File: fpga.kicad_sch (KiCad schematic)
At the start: 29 parts, among them U10 P0082_BOTTOMMOUNT, U11 SN75160BDW, U12 SN75160BDW, U13 SN75160BDW, U14 SN75160BDW

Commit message: Save work on simplifying the desing
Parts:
- removed U11, U12, U13, U14: SN75160BDW, Package_SO:SOIC-20W_7.5x12.8mm_P1.27mm, symbol Interface:SN75160BDW
- added R55, R56, R57, R58: 0R, Resistor_SMD:R_0402_1005Metric_Pad0.72x0.64mm_HandSolder, symbol Device:R
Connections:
- net D_ADC_A0: now also R95.1
- net D_ADC_A1: now also R96.1
- net D_ADC_A10: now also R105.1
- net D_ADC_A11: now also R106.1
- net D_ADC_A2: now also R97.1
- net D_ADC_A3: now also R98.1
- net D_ADC_A4: now also R99.1
- net D_ADC_A5: now also R100.1
- net D_ADC_A6: now also R101.1
- net D_ADC_A7: now also R102.1
- net D_ADC_A8: now also R103.1
- net D_ADC_A9: now also R104.1
- net D_ADC_B0: now also R107.1
- net D_ADC_B1: now also R108.1
- net D_ADC_B10: now also R117.1
- net D_ADC_B11: now also R118.1
- net D_ADC_B2: now also R109.1
- net D_ADC_B3: now also R110.1
- net D_ADC_B4: now also R111.1
- net D_ADC_B5: now also R112.1
- net D_ADC_B6: now also R113.1
- net D_ADC_B7: now also R114.1
- net D_ADC_B8: now also R115.1
- net D_ADC_B9: now also R116.1
- net at U10.JP1_11 (GPIO-0_VCC_SYS): now also R55.1
- net GND: now reaches U10.JP1_12 (GPIO-0_GND), U10.JP1_30 (GPIO-0_GND)
- net GND: now also U10.JP2_12 (GPIO-1_GND), U10.JP2_30 (GPIO-1_GND)
- net at U10.JP1_29 (GPIO-0_VCC3P3): now also R56.1
- net at U10.JP2_11 (GPIO-1_VCC_SYS): now also R57.1
- net at U10.JP2_29 (GPIO-1_VCC3P3): now also R58.1
- new net +3V3: R56.2, R58.2
- new net +5V: R55.2, R57.2
- no-connect marks 16 -> 0
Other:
- moved on the sheet: R100, R101, R102, R103, R104, R105, R106, R107, R108, R109, R110, R111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

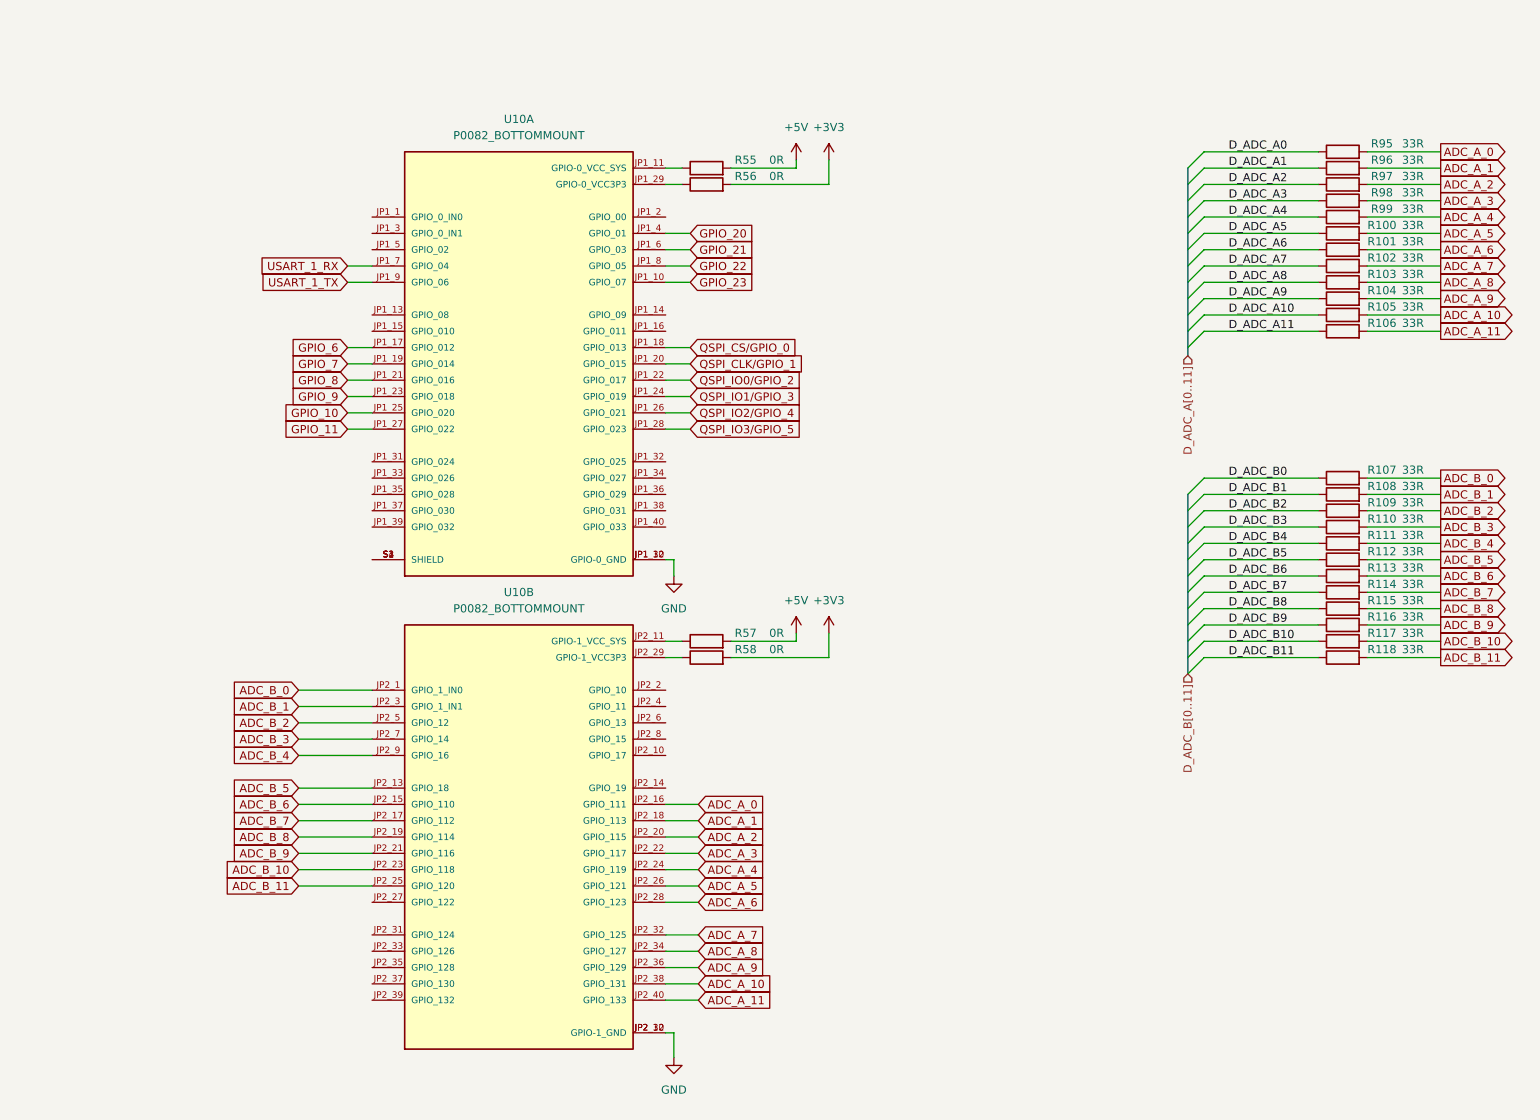
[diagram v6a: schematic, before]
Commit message: Simplifying the design
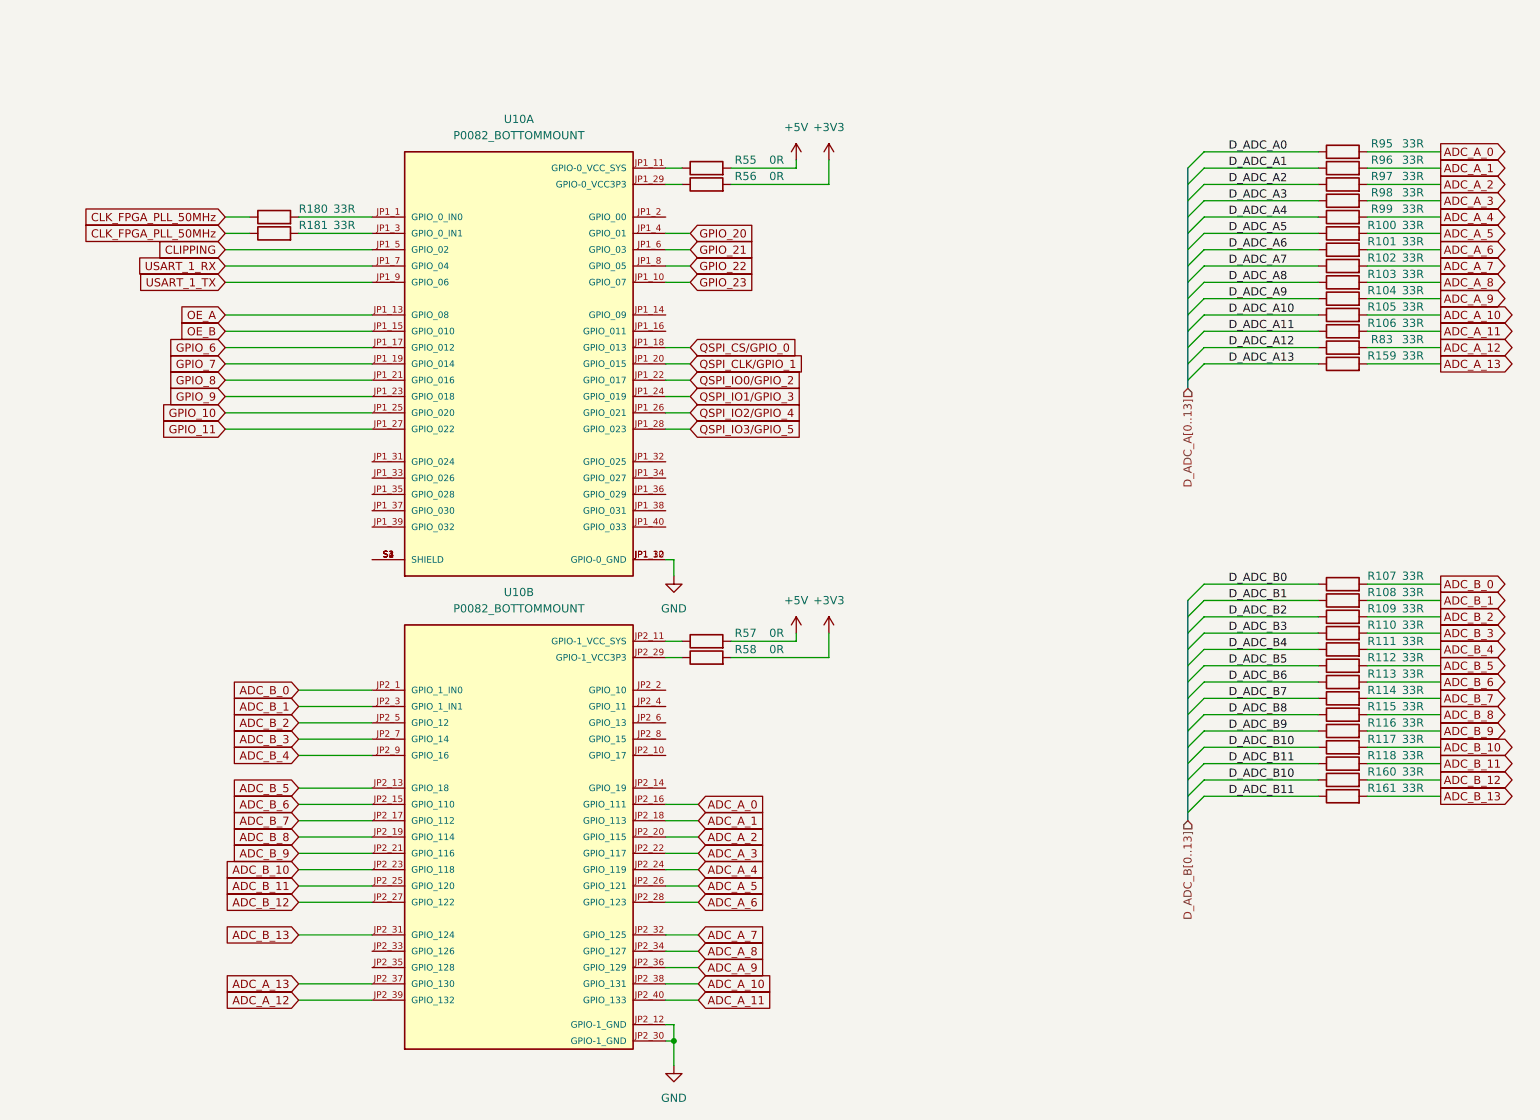
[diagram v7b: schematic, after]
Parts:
- added R159, R160, R161, R180, R181, R83: 33R, Resistor_SMD:R_0402_1005Metric_Pad0.72x0.64mm_HandSolder, symbol Device:R
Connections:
- net D_ADC_B10: now also R160.1
- net D_ADC_B11: now also R161.1
- net at U10.JP1_1 (GPIO_0_IN0): now also R180.2
- net OE_A: now reaches U10.JP1_13 (GPIO_08)
- net OE_B: now reaches U10.JP1_15 (GPIO_010)
- net at U10.JP1_3 (GPIO_0_IN1): now also R181.2
- net CLIPPING: now reaches U10.JP1_5 (GPIO_02)
- net ADC_B_12: now reaches U10.JP2_27 (GPIO_122)
- net ADC_B_12: now also R160.2
- net ADC_B_13: now reaches U10.JP2_31 (GPIO_124)
- net ADC_B_13: now also R161.2
- net ADC_A_13: now reaches U10.JP2_37 (GPIO_130)
- net ADC_A_13: now also R159.2
- net ADC_A_12: now reaches U10.JP2_39 (GPIO_132)
- net ADC_A_12: now also R83.2
- new net CLK_FPGA_PLL_50MHz: R180.1, R181.1
- new net D_ADC_A12: R83.1
- new net D_ADC_A13: R159.1
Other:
- moved on the sheet: R107, R108, R109, R110, R111, R112, R113, R114, R115, R116, R117, R118

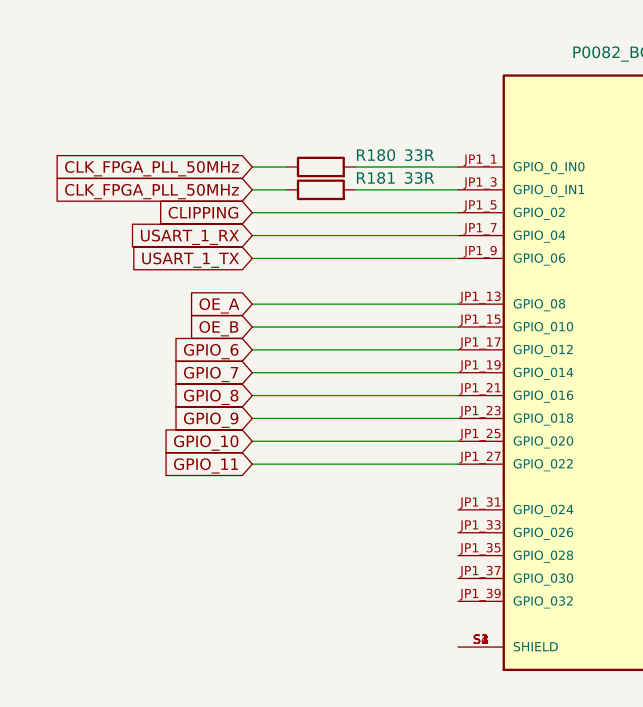
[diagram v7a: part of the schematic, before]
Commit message: Gain on diff amp 0.2
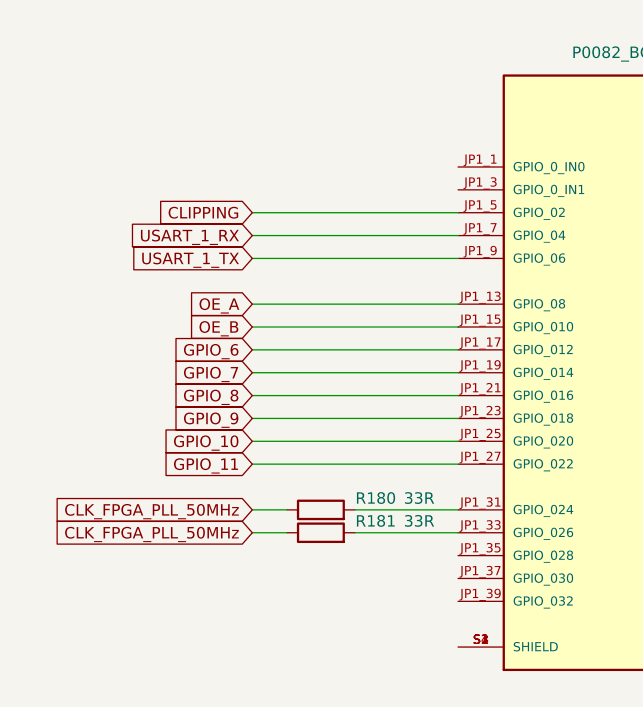
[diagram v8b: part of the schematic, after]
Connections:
- net at R181.2: now also U10.JP1_33 (GPIO_026); no longer U10.JP1_3 (GPIO_0_IN1)
- net at U10.JP1_1 (GPIO_0_IN0): no longer R180.2
- net at U10.JP1_31 (GPIO_024): now also R180.2
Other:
- moved on the sheet: R180, R181
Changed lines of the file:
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@@
 	(wire
 		(pts
-			(xy 234.95 54.61) (xy 246.38 54.61)
+			(xy 68.58 87.63) (xy 80.01 87.63)
 		)
 		(stroke
@@
 	(wire
 		(pts
-			(xy 130.81 143.51) (xy 125.73 143.51)
+			(xy 234.95 54.61) (xy 246.38 54.61)
 		)
 		(stroke
@@
 	(wire
 		(pts
-			(xy 68.58 135.89) (xy 80.01 135.89)
+			(xy 130.81 143.51) (xy 125.73 143.51)
 		)
 		(stroke
@@
 	(wire
 		(pts
-			(xy 130.81 140.97) (xy 125.73 140.97)
+			(xy 68.58 135.89) (xy 80.01 135.89)
 		)
 		(stroke
@@
 	(wire
 		(pts
-			(xy 129.54 77.47) (xy 125.73 77.47)
+			(xy 130.81 140.97) (xy 125.73 140.97)
 		)
 		(stroke
@@
 	(wire
 		(pts
-			(xy 68.58 46.99) (xy 80.01 46.99)
+			(xy 129.54 77.47) (xy 125.73 77.47)
 		)
 		(stroke
@@
 	(wire
 		(pts
-			(xy 60.96 46.99) (xy 57.15 46.99)
-		)
-		(stroke
-			(width 0)
-			(type default)
-		)
-	)
-	(wire
-		(pts
 			(xy 209.55 67.31) (xy 227.33 67.31)
 		)
@@
 		)
 	)
-	(wire
-		(pts
-			(xy 60.96 49.53) (xy 57.15 49.53)
-		)
-		(stroke
-			(width 0)
-			(type default)
-		)
-	)
 	(bus
 		(pts
@@
 	(wire
 		(pts
-			(xy 68.58 49.53) (xy 80.01 49.53)
-		)
-		(stroke
-			(width 0)
-			(type default)
-		)
-	)
-	(wire
-		(pts
 			(xy 68.58 140.97) (xy 80.01 140.97)
 		)
@@
 	(wire
 		(pts
+			(xy 60.96 85.09) (xy 57.15 85.09)
+		)
+		(stroke
+			(width 0)
+			(type default)
+		)
+	)
+	(wire
+		(pts
+			(xy 60.96 87.63) (xy 57.15 87.63)
+		)
+		(stroke
+			(width 0)
+			(type default)
+		)
+	)
+	(wire
+		(pts
 			(xy 130.81 161.29) (xy 125.73 161.29)
 		)
@@
 		)
 	)
+	(wire
+		(pts
+			(xy 68.58 85.09) (xy 80.01 85.09)
+		)
+		(stroke
+			(width 0)
+			(type default)
+		)
+	)
 	(bus
 		(pts
@@
 		)
 	)
-	(global_label "CLK_FPGA_PLL_50MHz"
+	(global_label "OE_B"
 		(shape input)
-		(at 57.15 46.99 180)
+		(at 57.15 64.77 180)
 		(fields_autoplaced yes)
 		(effects
@@
 		)
 		(property "Intersheetrefs" "${INTERSHEET_REFS}"
-			(at 33.4215 46.99 0)
+			(at 49.4477 64.77 0)
 			(effects
 				(font
@@
 		)
 	)
-	(global_label "OE_B"
-		(shape input)
-		(at 57.15 64.77 180)
+	(global_label "ADC_B_11"
+		(shape output)
+		(at 246.38 132.08 0)
 		(fields_autoplaced yes)
 		(effects
@@
 				(size 1.27 1.27)
 			)
-			(justify right)
+			(justify left)
 		)
 		(property "Intersheetrefs" "${INTERSHEET_REFS}"
-			(at 49.4477 64.77 0)
+			(at 258.618 132.08 0)
 			(effects
 				(font
 					(size 1.27 1.27)
 				)
-				(justify right)
+				(justify left)
 				(hide yes)
 			)
 		)
 	)
-	(global_label "ADC_B_11"
+	(global_label "ADC_A_10"
 		(shape output)
-		(at 246.38 132.08 0)
+		(at 246.38 62.23 0)
 		(fields_autoplaced yes)
 		(effects
@@
 		)
 		(property "Intersheetrefs" "${INTERSHEET_REFS}"
-			(at 258.618 132.08 0)
+			(at 258.4366 62.23 0)
 			(effects
 				(font
@@
 		)
 	)
-	(global_label "ADC_A_10"
-		(shape output)
-		(at 246.38 62.23 0)
+	(global_label "CLK_FPGA_PLL_50MHz"
+		(shape input)
+		(at 57.15 87.63 180)
 		(fields_autoplaced yes)
 		(effects
@@
 				(size 1.27 1.27)
 			)
-			(justify left)
+			(justify right)
 		)
 		(property "Intersheetrefs" "${INTERSHEET_REFS}"
-			(at 258.4366 62.23 0)
+			(at 33.4215 87.63 0)
 			(effects
 				(font
 					(size 1.27 1.27)
 				)
-				(justify left)
+				(justify right)
 				(hide yes)
 			)
@@
 		)
 	)
-	(global_label "CLK_FPGA_PLL_50MHz"
+	(global_label "QSPI_IO3{slash}GPIO_5"
 		(shape input)
-		(at 57.15 49.53 180)
+		(at 129.54 80.01 0)
 		(fields_autoplaced yes)
 		(effects
@@
 				(size 1.27 1.27)
 			)
-			(justify right)
+			(justify left)
 		)
 		(property "Intersheetrefs" "${INTERSHEET_REFS}"
-			(at 33.4215 49.53 0)
+			(at 149.0353 80.01 0)
 			(effects
 				(font
 					(size 1.27 1.27)
 				)
-				(justify right)
+				(justify left)
 				(hide yes)
 			)
 		)
 	)
-	(global_label "QSPI_IO3{slash}GPIO_5"
+	(global_label "QSPI_IO1{slash}GPIO_3"
 		(shape input)
-		(at 129.54 80.01 0)
+		(at 129.54 74.93 0)
 		(fields_autoplaced yes)
 		(effects
@@
 		)
 		(property "Intersheetrefs" "${INTERSHEET_REFS}"
-			(at 149.0353 80.01 0)
+			(at 149.0353 74.93 0)
 			(effects
 				(font
@@
 		)
 	)
-	(global_label "QSPI_IO1{slash}GPIO_3"
+	(global_label "GPIO_21"
 		(shape input)
-		(at 129.54 74.93 0)
+		(at 129.54 52.07 0)
 		(fields_autoplaced yes)
 		(effects
@@
 		)
 		(property "Intersheetrefs" "${INTERSHEET_REFS}"
-			(at 149.0353 74.93 0)
+			(at 140.3871 52.07 0)
 			(effects
 				(font
@@
 		)
 	)
-	(global_label "GPIO_21"
+	(global_label "ADC_A_6"
 		(shape input)
-		(at 129.54 52.07 0)
+		(at 130.81 153.67 0)
 		(fields_autoplaced yes)
 		(effects
@@
 		)
 		(property "Intersheetrefs" "${INTERSHEET_REFS}"
-			(at 140.3871 52.07 0)
+			(at 141.6571 153.67 0)
 			(effects
 				(font
@@
 		)
 	)
-	(global_label "ADC_A_6"
+	(global_label "CLK_FPGA_PLL_50MHz"
 		(shape input)
-		(at 130.81 153.67 0)
+		(at 57.15 85.09 180)
 		(fields_autoplaced yes)
 		(effects
@@
 				(size 1.27 1.27)
 			)
-			(justify left)
+			(justify right)
 		)
 		(property "Intersheetrefs" "${INTERSHEET_REFS}"
-			(at 141.6571 153.67 0)
+			(at 33.4215 85.09 0)
 			(effects
 				(font
 					(size 1.27 1.27)
 				)
-				(justify left)
+				(justify right)
 				(hide yes)
 			)
@@
 	(symbol
 		(lib_id "Device:R")
-		(at 64.77 49.53 90)
+		(at 64.77 87.63 90)
 		(unit 1)
 		(exclude_from_sim no)
@@
 		(dnp no)
 		(property "Reference" "R181"
-			(at 70.866 48.26 90)
+			(at 70.866 86.36 90)
 			(effects
 				(font
@@
 		)
 		(property "Value" "33R"
-			(at 75.692 48.26 90)
+			(at 75.692 86.36 90)
 			(effects
 				(font
@@
 		)
 		(property "Footprint" "Resistor_SMD:R_0402_1005Metric_Pad0.72x0.64mm_HandSolder"
-			(at 64.77 51.308 90)
+			(at 64.77 89.408 90)
 			(effects
 				(font
@@
 		)
 		(property "Datasheet" "~"
-			(at 64.77 49.53 0)
+			(at 64.77 87.63 0)
 			(effects
 				(font
@@
 		)
 		(property "Description" "Resistor"
-			(at 64.77 49.53 0)
+			(at 64.77 87.63 0)
 			(effects
 				(font
@@
 	(symbol
 		(lib_id "Device:R")
-		(at 64.77 46.99 90)
+		(at 64.77 85.09 90)
 		(unit 1)
 		(exclude_from_sim no)
@@
 		(dnp no)
 		(property "Reference" "R180"
-			(at 70.866 45.72 90)
+			(at 70.866 83.82 90)
 			(effects
 				(font
@@
 		)
 		(property "Value" "33R"
-			(at 75.692 45.72 90)
+			(at 75.692 83.82 90)
 			(effects
 				(font
@@
 		)
 		(property "Footprint" "Resistor_SMD:R_0402_1005Metric_Pad0.72x0.64mm_HandSolder"
-			(at 64.77 48.768 90)
+			(at 64.77 86.868 90)
 			(effects
 				(font
@@
 		)
 		(property "Datasheet" "~"
-			(at 64.77 46.99 0)
+			(at 64.77 85.09 0)
 			(effects
 				(font
@@
 		)
 		(property "Description" "Resistor"
-			(at 64.77 46.99 0)
+			(at 64.77 85.09 0)
 			(effects
 				(font
